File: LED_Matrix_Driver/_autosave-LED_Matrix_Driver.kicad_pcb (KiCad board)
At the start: 4 copper layers, 76 parts, among them J1 Audio In, J2 Screw_Terminal_01x02, J3 Buttons, J4 LED Anode Rows, J5 Columns 24-31 LED Cathodes, J6 Columns 16-23 LED Cathodes, J7 Columns 8-15 LED Cathodes, J8 Columns 0-7 LED Cathodes, U1 ESP32-DEVKITC-32E, U2 74HCT244, U3 MIC2981, U4 74HC238, U5 HEF4794B, U6 HEF4794B, U7 HEF4794B, U8 HEF4794B

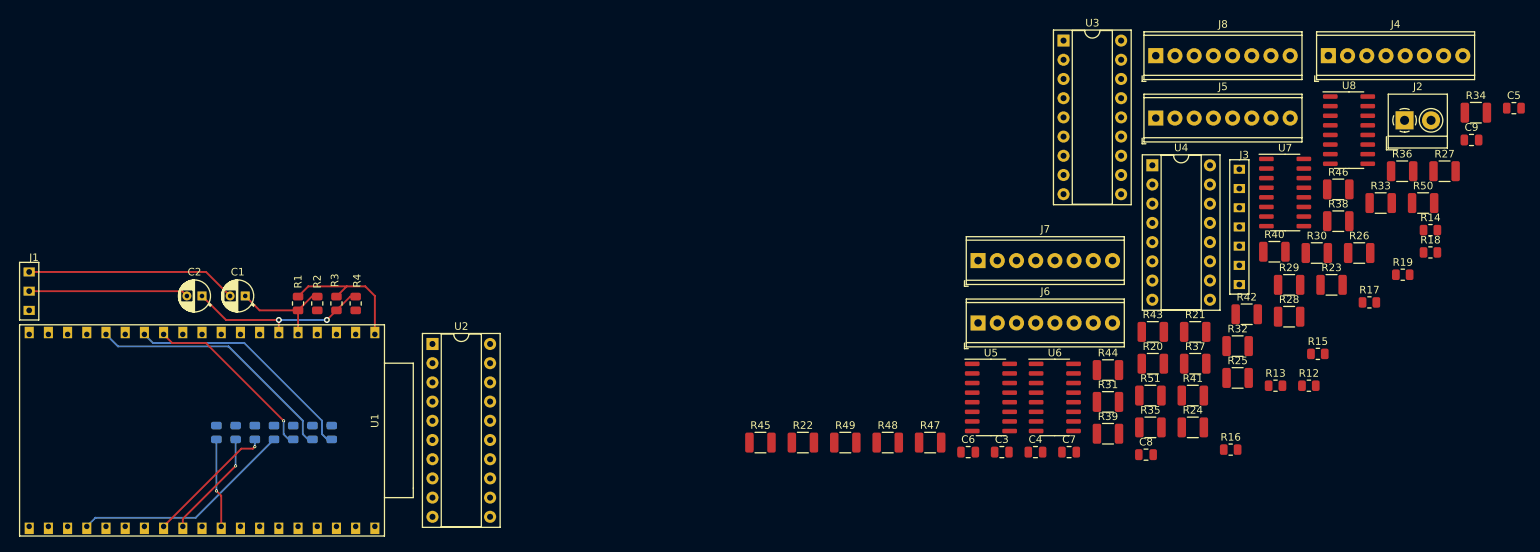
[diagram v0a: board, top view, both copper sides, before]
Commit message: Modification of LED_Matrix_Driver to use SMD components
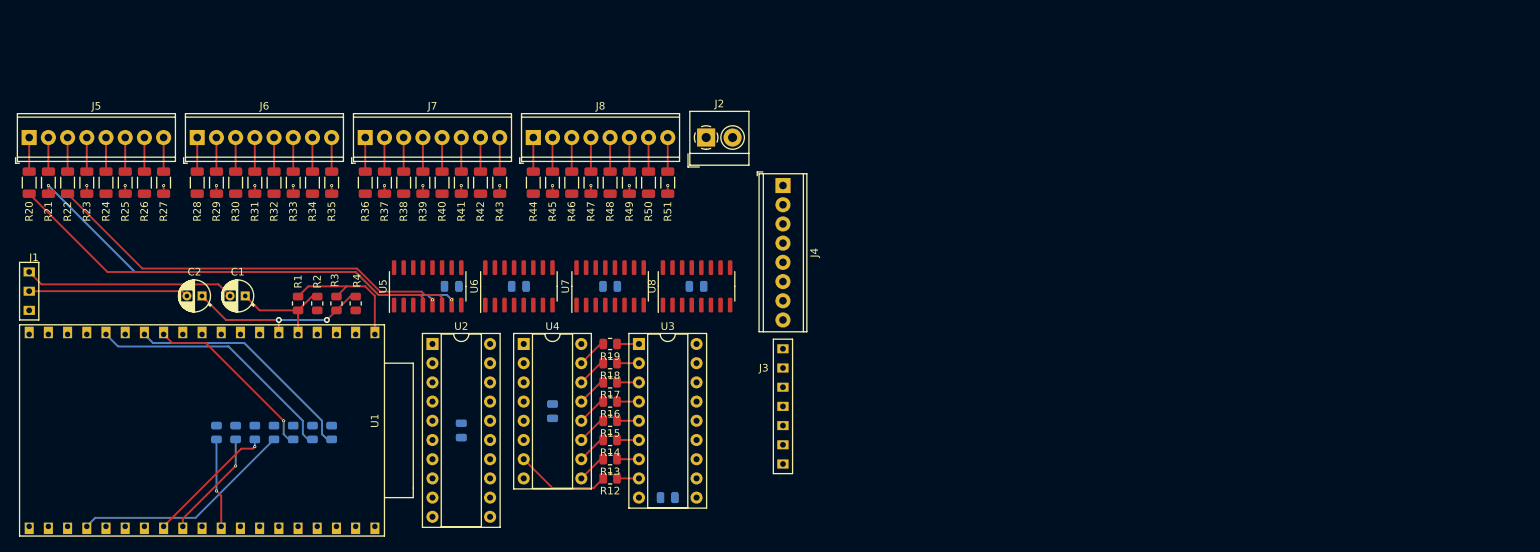
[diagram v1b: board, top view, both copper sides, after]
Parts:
- C3, C4, C5, C6, C7, C8, C9: moved to B.Cu
- R20, R21, R22, R23, R24, R25, R26, R27, R28, R29, R30, R31, R32, R33, R34, R35, R36, R37, R38, R39, R40, R41, R42, R43, R44, R45, R46, R47, R48, R49, R50, R51: footprint Resistor_SMD:R_1210_3225Metric -> Resistor_SMD:R_1206_3216Metric
- moved R27 169.4 mm to (32.4, 89.2), turned to 270 degrees
- moved R23 165.2 mm to (22.2, 89.2), turned to 270 degrees
- moved R26 160.9 mm to (29.8, 89.2), turned to 270 degrees
- moved R34 154.2 mm to (52.1, 89.2), turned to 270 degrees
- moved R21 153.0 mm to (17.1, 89.2), turned to 270 degrees
- moved R20 150.5 mm to (14.6, 89.2), turned to 270 degrees
- moved R25 149.4 mm to (27.3, 89.2), turned to 270 degrees
- moved J5 149.0 mm to (14.6, 83.2)
- moved R24 147.3 mm to (24.8, 89.2), turned to 270 degrees
- moved R28 145.5 mm to (36.8, 89.2), turned to 270 degrees
- moved R33 143.9 mm to (49.5, 89.2), turned to 270 degrees
- moved R30 143.3 mm to (41.9, 89.2), turned to 270 degrees
- moved R29 142.5 mm to (39.4, 89.2), turned to 270 degrees
- moved R36 137.1 mm to (59.1, 89.2), turned to 270 degrees
- moved C5 133.3 mm to (83.8, 119.4), turned to 270 degrees
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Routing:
- net Net-(R20-Pad2): track 0.00 -> 58.7 mm
- net Net-(R21-Pad2): track 0.00 -> 58.1 mm, vias 0 -> 2
- net Net-(R22-Pad2): track 0.00 -> 56.2 mm
- net Net-(R12-Pad2): track 0.00 -> 12.6 mm
- net Net-(J8-Pad8): track 0.00 -> 4.51 mm
- net Net-(J8-Pad7): track 0.00 -> 4.51 mm
- net Net-(J8-Pad6): track 0.00 -> 4.51 mm
- net Net-(J8-Pad5): track 0.00 -> 4.51 mm
- net Net-(J8-Pad4): track 0.00 -> 4.51 mm
- net Net-(J8-Pad3): track 0.00 -> 4.51 mm
- net Net-(J8-Pad2): track 0.00 -> 4.51 mm
- net Net-(J8-Pad1): track 0.00 -> 4.51 mm
- net Net-(J7-Pad8): track 0.00 -> 4.51 mm
- net Net-(J7-Pad7): track 0.00 -> 4.51 mm
- net Net-(J7-Pad6): track 0.00 -> 4.51 mm
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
